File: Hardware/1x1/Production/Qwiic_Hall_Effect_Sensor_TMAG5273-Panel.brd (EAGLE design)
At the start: 123.2 x 117.3 mm, 790 parts, among them J1 QWIIC_RIGHT_ANGLE, J10 QWIIC_RIGHT_ANGLE, J11 QWIIC_RIGHT_ANGLE, J13 QWIIC_RIGHT_ANGLE, J14 QWIIC_RIGHT_ANGLE, J16 QWIIC_RIGHT_ANGLE, J17 QWIIC_RIGHT_ANGLE, J19 QWIIC_RIGHT_ANGLE, J2 QWIIC_RIGHT_ANGLE, J20 QWIIC_RIGHT_ANGLE, J22 QWIIC_RIGHT_ANGLE, J23 QWIIC_RIGHT_ANGLE, J25 QWIIC_RIGHT_ANGLE, J26 QWIIC_RIGHT_ANGLE, J28 QWIIC_RIGHT_ANGLE, J29 QWIIC_RIGHT_ANGLE, J31 QWIIC_RIGHT_ANGLE, J32 QWIIC_RIGHT_ANGLE, J34 QWIIC_RIGHT_ANGLE, J35 QWIIC_RIGHT_ANGLE, J37 QWIIC_RIGHT_ANGLE, J38 QWIIC_RIGHT_ANGLE, J4 QWIIC_RIGHT_ANGLE, J40 QWIIC_RIGHT_ANGLE, J41 QWIIC_RIGHT_ANGLE, J43 QWIIC_RIGHT_ANGLE, J44 QWIIC_RIGHT_ANGLE, J46 QWIIC_RIGHT_ANGLE, J47 QWIIC_RIGHT_ANGLE, J5 QWIIC_RIGHT_ANGLE, J7 QWIIC_RIGHT_ANGLE, J8 QWIIC_RIGHT_ANGLE, Q1 20V/4.2A/52mΩ/1.4W, Q10 20V/4.2A/52mΩ/1.4W, Q11 20V/4.2A/52mΩ/1.4W, Q12 20V/4.2A/52mΩ/1.4W, Q13 20V/4.2A/52mΩ/1.4W, Q14 20V/4.2A/52mΩ/1.4W, Q15 20V/4.2A/52mΩ/1.4W, Q16 20V/4.2A/52mΩ/1.4W, Q2 20V/4.2A/52mΩ/1.4W, Q3 20V/4.2A/52mΩ/1.4W, Q4 20V/4.2A/52mΩ/1.4W, Q5 20V/4.2A/52mΩ/1.4W, Q6 20V/4.2A/52mΩ/1.4W, Q7 20V/4.2A/52mΩ/1.4W, Q8 20V/4.2A/52mΩ/1.4W, Q9 20V/4.2A/52mΩ/1.4W, U1 TMAG5273, U10 TMAG5273, U11 TMAG5273, U12 TMAG5273, U13 TMAG5273, U14 TMAG5273, U15 TMAG5273, U16 TMAG5273, U2 TMAG5273, U3 TMAG5273, U4 TMAG5273, U5 TMAG5273, U6 TMAG5273, U7 TMAG5273, U8 TMAG5273, U9 TMAG5273

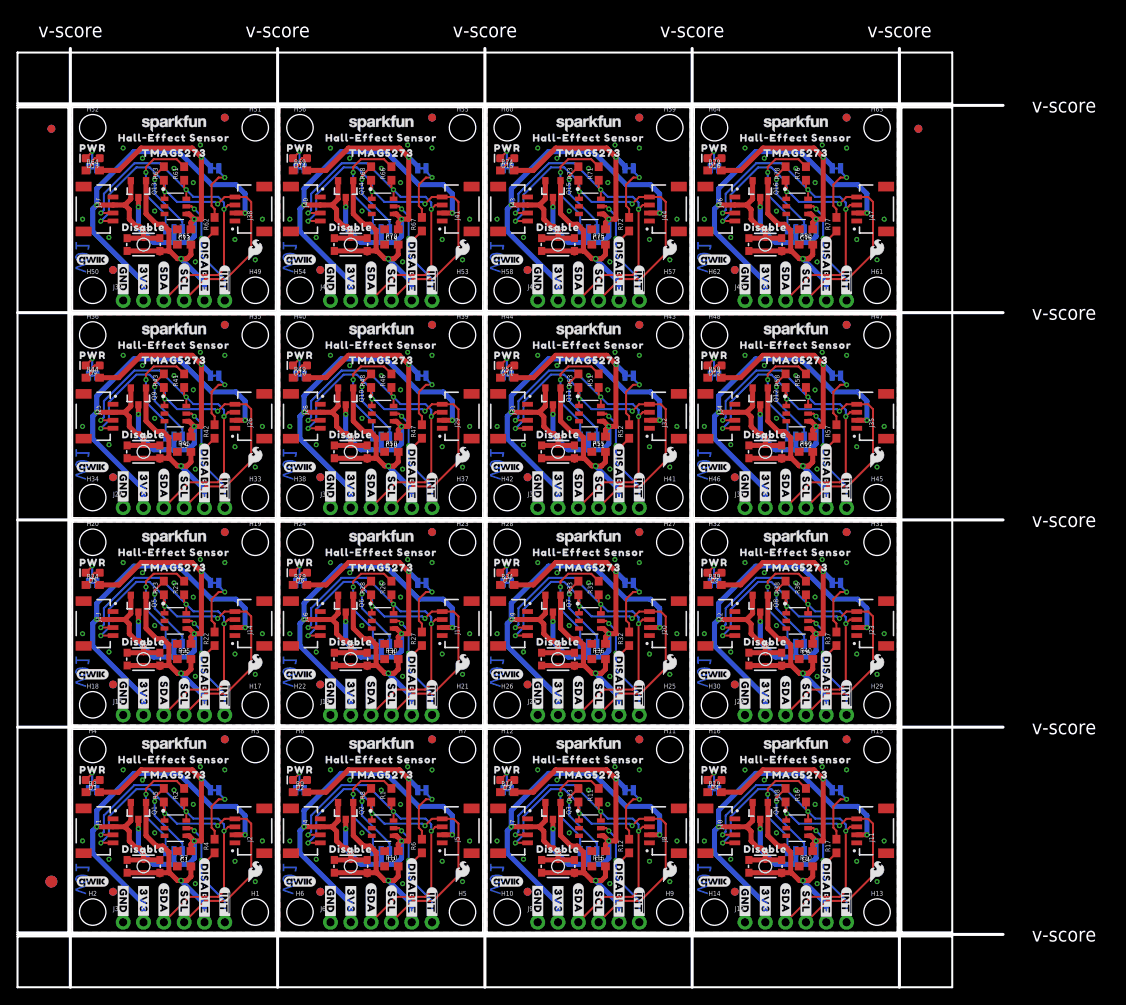
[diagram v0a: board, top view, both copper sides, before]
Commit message: Files for ordering
Re-added the correct panel files for the project along with ordering instructions. Made final adjustments from design review and board is ready for order!
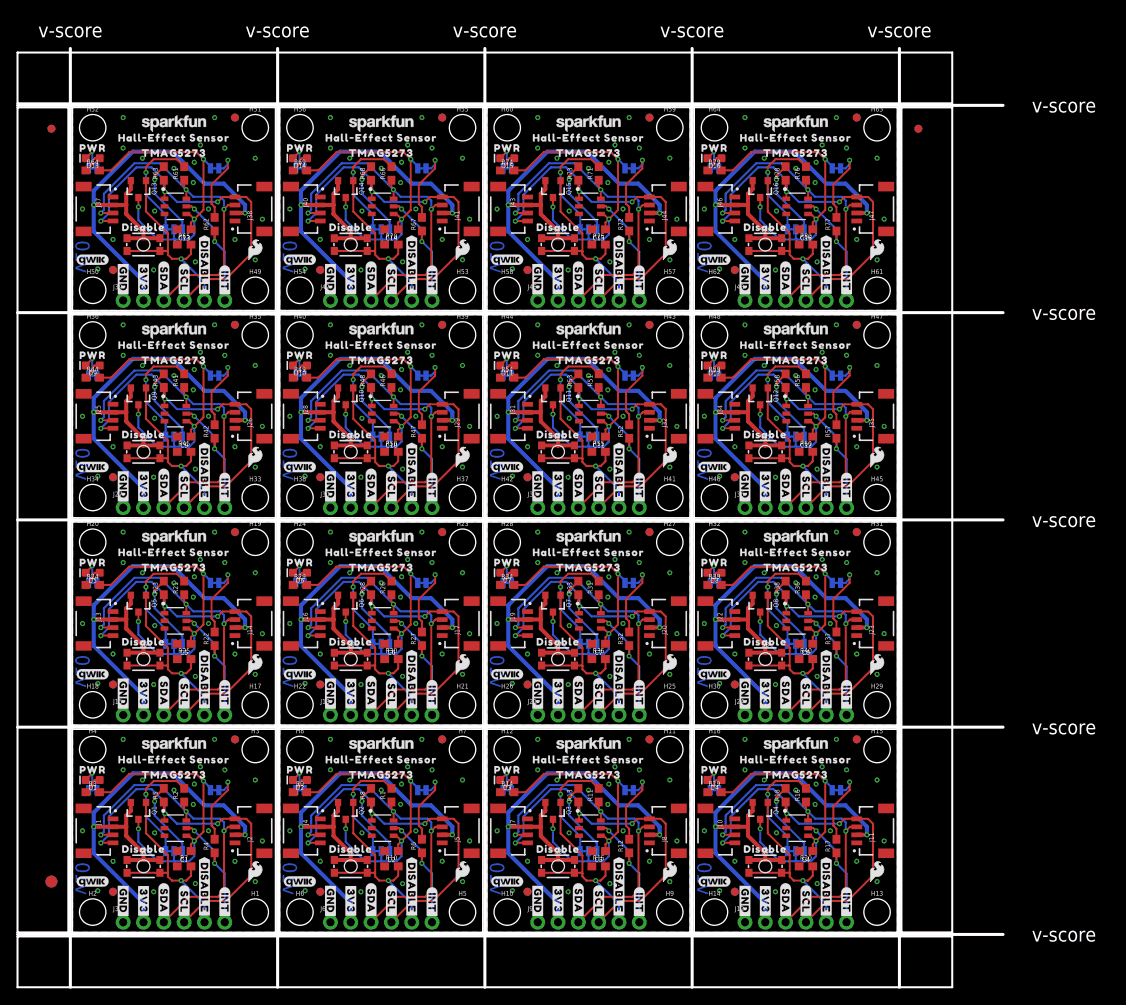
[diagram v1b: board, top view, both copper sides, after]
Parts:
- removed JP17, JP20, JP23, JP26, JP29, JP32, JP35, JP38, JP41, JP44, JP47: JUMPER-SMT_2_NC_TRACE_SILK, SparkFun-Jumpers:SMT-JUMPER_2_NC_TRACE_SILK
- added I2C, I2C1, I2C2, I2C3, I2C4, I2C5: JUMPER-SMT_3_2-NC_TRACE_SILK, SparkFun-Jumpers:SMT-JUMPER_3_2-NC_TRACE_SILK
- added LED, LED1, LED2, LED3, LED4: JUMPER-SMT_2_NC_TRACE_SILK, SparkFun-Jumpers:SMT-JUMPER_2_NC_TRACE_SILK
- JP1, JP10, JP13, JP16, JP4, JP7: value JUMPER-SMT_3_2-NC_TRACE_SILK -> JUMPER-SMT_2_NC_TRACE_SILK; device SparkFun-Jumpers:SMT-JUMPER_3_2-NC_TRACE_SILK -> SparkFun-Jumpers:SMT-JUMPER_2_NC_TRACE_SILK
- U$100, U$120, U$140, U$160, U$180, U$200, U$220, U$240, U$260, U$280, U$300, U$320, U$40, U$60, U$80: device output:DISABLE5281 -> output:#DISABLE#5290
- U$107, U$127, U$147, U$167, U$187, U$207, U$227, U$247, U$267, U$27, U$287, U$307, U$47, U$67, U$87: device output:##INT#43 -> output:#I�C#0
- U$108, U$128, U$148, U$168, U$188, U$208, U$228, U$248, U$268, U$28, U$288, U$308, U$48, U$68, U$88: device output:#I�C#0 -> output:HALL#EFFECT_SENSOR45
- U$109, U$129, U$149, U$169, U$189, U$209, U$229, U$249, U$269, U$289, U$29, U$309, U$49, U$69, U$89: device output:HALL#EFFECT_SENSOR45 -> output:TMAG527346
- U$110, U$130, U$150, U$170, U$190, U$210, U$230, U$250, U$270, U$290, U$30, U$310, U$50, U$70, U$90: device output:TMAG527346 -> output:#SDA#5280
- U$111, U$131, U$151, U$171, U$191, U$211, U$231, U$251, U$271, U$291, U$31, U$311, U$51, U$71, U$91: device output:#SDA#5280 -> output:#SCL#5281
- U$112, U$132, U$152, U$172, U$192, U$212, U$232, U$252, U$272, U$292, U$312, U$32, U$52, U$72, U$92: device output:#SCL#5281 -> output:#3V3#0
- U$113, U$133, U$153, U$173, U$193, U$213, U$233, U$253, U$273, U$293, U$313, U$33, U$53, U$73, U$93: device output:#3V3#0 -> output:#GND#4
- U$114, U$134, U$154, U$174, U$194, U$214, U$234, U$254, U$274, U$294, U$314, U$34, U$54, U$74, U$94: device output:#GND#4 -> output:TMAG5273_HALL#EFFECT_SENSOR5
- U$115, U$135, U$155, U$175, U$195, U$215, U$235, U$255, U$275, U$295, U$315, U$35, U$55, U$75, U$95: device output:TMAG5273_HALL#EFFECT_SENSOR5 -> output:DISABLE5281
- U$116, U$117, U$136, U$137, U$156, U$157, U$176, U$177, U$196, U$197, U$216, U$217, U$236, U$237, U$256, U$257, U$276, U$277, U$296, U$297, U$316, U$317, U$36, U$37, U$56, U$57, U$76, U$77, U$96, U$97: device output:##INT#5276 -> output:#INT#5285
- U$118, U$138, U$158, U$178, U$198, U$218, U$238, U$258, U$278, U$298, U$318, U$38, U$58, U$78, U$98: device output:#DISABLE#5280 -> output:#INT#5289
- U$119, U$139, U$159, U$179, U$199, U$219, U$239, U$259, U$279, U$299, U$319, U$39, U$59, U$79, U$99: device output:#DISABLE#5280 -> output:#DISABLE#5290
- U$15: device output:##INT#5276 -> output:#DISABLE#5290
- U$17, U$5: device output:#DISABLE#5280 -> output:#INT#5285
- U$6: device output:##INT#5276 -> output:#INT#5289
- U$9: device output:##INT#43 -> output:#DISABLE#5290
- moved JP15 84.7 mm to (69.6, 95.5)
- moved JP16 82.3 mm to (95.5, 95.5)
- moved JP10 75.6 mm to (43.7, 69.6)
- moved JP3 67.1 mm to (69.6, 17.8)
- moved JP9 63.4 mm to (17.8, 69.6)
- moved JP13 59.7 mm to (17.8, 95.5)
- moved JP11 57.9 mm to (69.6, 69.6)
- moved JP14 57.9 mm to (43.7, 95.5)
- moved JP4 57.4 mm to (95.5, 17.8)
- moved JP12 54.0 mm to (95.5, 69.6)
- moved JP5 36.6 mm to (17.8, 43.7)
- moved JP8 36.6 mm to (95.5, 43.7)
- moved JP7 33.9 mm to (69.6, 43.7)
- moved JP1 31.9 mm to (43.7, 17.8)
- moved JP6 30.1 mm to (43.7, 43.7)
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- renumbered JP18 to LED5, JP19 to I2C6, JP21 to LED6, JP22 to I2C7, JP24 to LED7, JP25 to I2C8, JP27 to LED8, JP28 to I2C9, JP30 to LED9, JP31 to I2C10, JP33 to LED10, JP34 to I2C11, JP36 to LED11, JP37 to I2C12, JP39 to LED12, JP40 to I2C13, JP42 to LED13, JP43 to I2C14, JP45 to LED14, JP46 to I2C15, JP48 to LED15
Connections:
- net 3.3V_SW: now also I2C.2; no longer JP1.2
- net 3.3V_SW1: now also I2C1.2, JP1.2; no longer JP4.2, JP5.2
- net 3.3V_SW10: now also JP11.2; no longer JP32.2
- net 3.3V_SW11: now also JP12.2; no longer JP35.2
- net 3.3V_SW12: now also JP13.2; no longer JP38.2
- net 3.3V_SW13: now also JP14.2; no longer JP41.2
- net 3.3V_SW14: now also JP15.2; no longer JP44.2
- net 3.3V_SW15: now also JP16.2; no longer JP47.2
- net 3.3V_SW2: now also I2C2.2, JP3.2; no longer JP7.2, JP8.2
- net 3.3V_SW3: now also I2C3.2, JP4.2; no longer JP10.2, JP11.2
- net 3.3V_SW4: now also I2C4.2, JP5.2; no longer JP13.2, JP14.2
- net 3.3V_SW5: now also I2C5.2, JP6.2; no longer JP16.2, JP17.2
- net 3.3V_SW6: now also JP7.2; no longer JP20.2
- net 3.3V_SW7: now also JP8.2; no longer JP23.2
- net 3.3V_SW8: now also JP9.2; no longer JP26.2
- net 3.3V_SW9: now also JP10.2; no longer JP29.2
- net GND: now also LED.1; no longer JP3.1
- net GND1: now also LED1.1; no longer JP6.1
- net GND2: now also LED2.1; no longer JP9.1
- net GND3: now also LED3.1; no longer JP12.1
- net GND4: now also LED4.1; no longer JP15.1
- net N$1: now also LED.2; no longer JP3.2
- net N$10: now also I2C1.1; no longer JP4.1
- net N$12: now also LED2.2; no longer JP9.2
- net N$13: now also JP3.1; no longer JP8.1
- net N$14: now also I2C2.3; no longer JP7.3
- net N$15: now also I2C2.1; no longer JP7.1
- net N$17: now also LED3.2; no longer JP12.2
- net N$18: now also JP4.1; no longer JP11.1
- net N$19: now also I2C3.3; no longer JP10.3
- net N$2: now also I2C.3; no longer JP1.3
- net N$20: now also I2C3.1; no longer JP10.1
- net N$22: now also LED4.2; no longer JP15.2
- net N$23: now also JP5.1; no longer JP14.1
- net N$24: now also I2C4.3; no longer JP13.3
- net N$25: now also I2C4.1; no longer JP13.1
- net N$28: now also JP6.1; no longer JP17.1
- net N$29: now also I2C5.3; no longer JP16.3
- net N$30: now also I2C5.1; no longer JP16.1
- net N$33: now also JP7.1; no longer JP20.1
- net N$38: now also JP8.1; no longer JP23.1
- net N$43: now also JP9.1; no longer JP26.1
- net N$48: now also JP10.1; no longer JP29.1
- net N$53: now also JP11.1; no longer JP32.1
- net N$58: now also JP12.1; no longer JP35.1
- net N$6: now also I2C.1; no longer JP1.1
- net N$63: now also JP13.1; no longer JP38.1
- net N$68: now also JP14.1; no longer JP41.1
- net N$7: now also LED1.2; no longer JP6.2
- net N$73: now also JP15.1; no longer JP44.1
- net N$78: now also JP16.1; no longer JP47.1
- net N$8: now also JP1.1; no longer JP5.1
- net N$9: now also I2C1.3; no longer JP4.3
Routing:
- net 3.3V_SW7: track 43.3 -> 40.8 mm
- net 3.3V_SW6: track 43.3 -> 40.8 mm
- net 3.3V_SW4: track 43.3 -> 40.8 mm
- net 3.3V_SW3: track 43.3 -> 40.8 mm
- net 3.3V_SW: track 43.3 -> 40.8 mm
- net 3.3V_SW2: track 43.3 -> 40.8 mm
- net 3.3V_SW5: track 43.3 -> 40.8 mm
- net 3.3V_SW15: track 43.3 -> 40.8 mm
- net 3.3V_SW10: track 43.3 -> 40.8 mm
- net 3.3V_SW14: track 43.3 -> 40.8 mm
- net 3.3V_SW11: track 43.3 -> 40.8 mm
- net 3.3V_SW1: track 43.3 -> 40.8 mm
- net 3.3V_SW9: track 43.3 -> 40.8 mm
- net 3.3V_SW8: track 43.3 -> 40.8 mm
- net 3.3V_SW12: track 43.3 -> 40.8 mm
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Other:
- board text added: "v10"
- board text removed: "v01"
